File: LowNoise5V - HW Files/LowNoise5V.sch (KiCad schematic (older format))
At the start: 10 parts

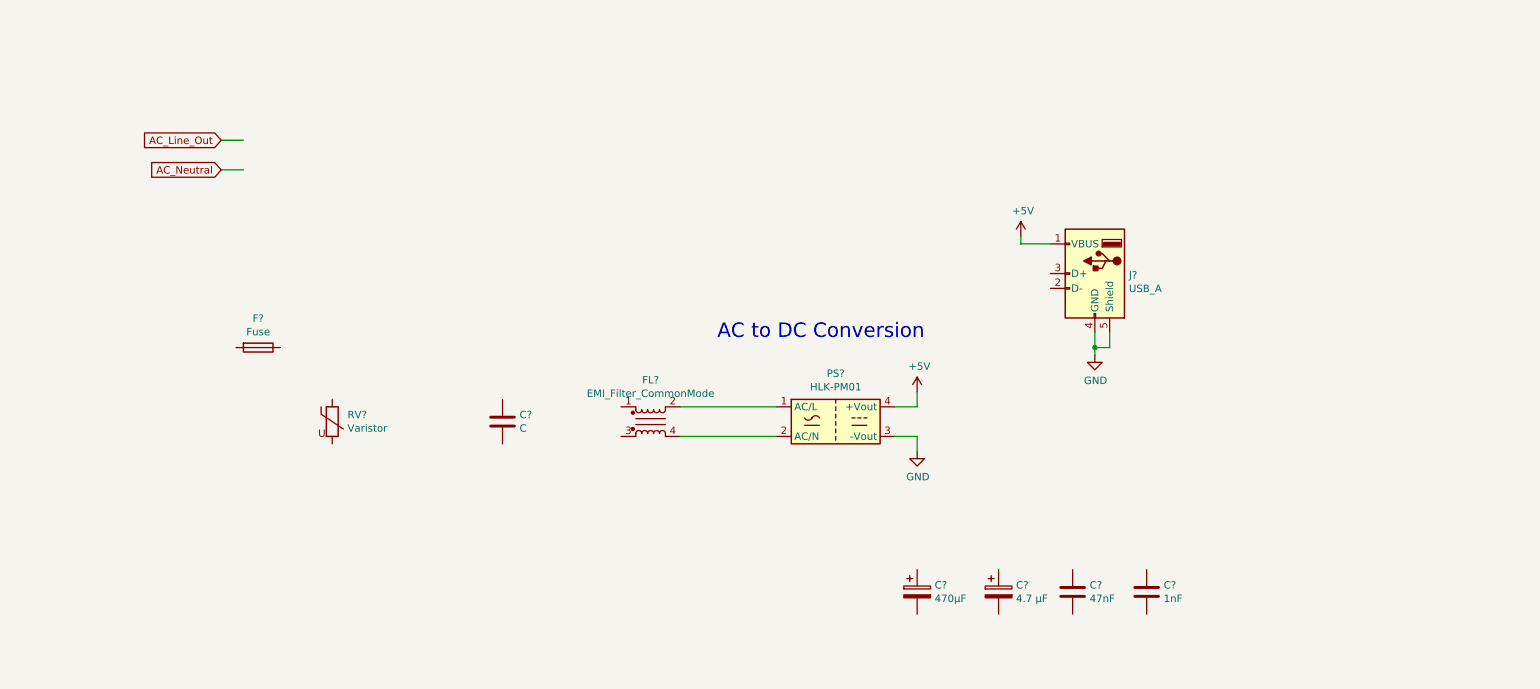
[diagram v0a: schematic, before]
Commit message: Update AC side components with part info
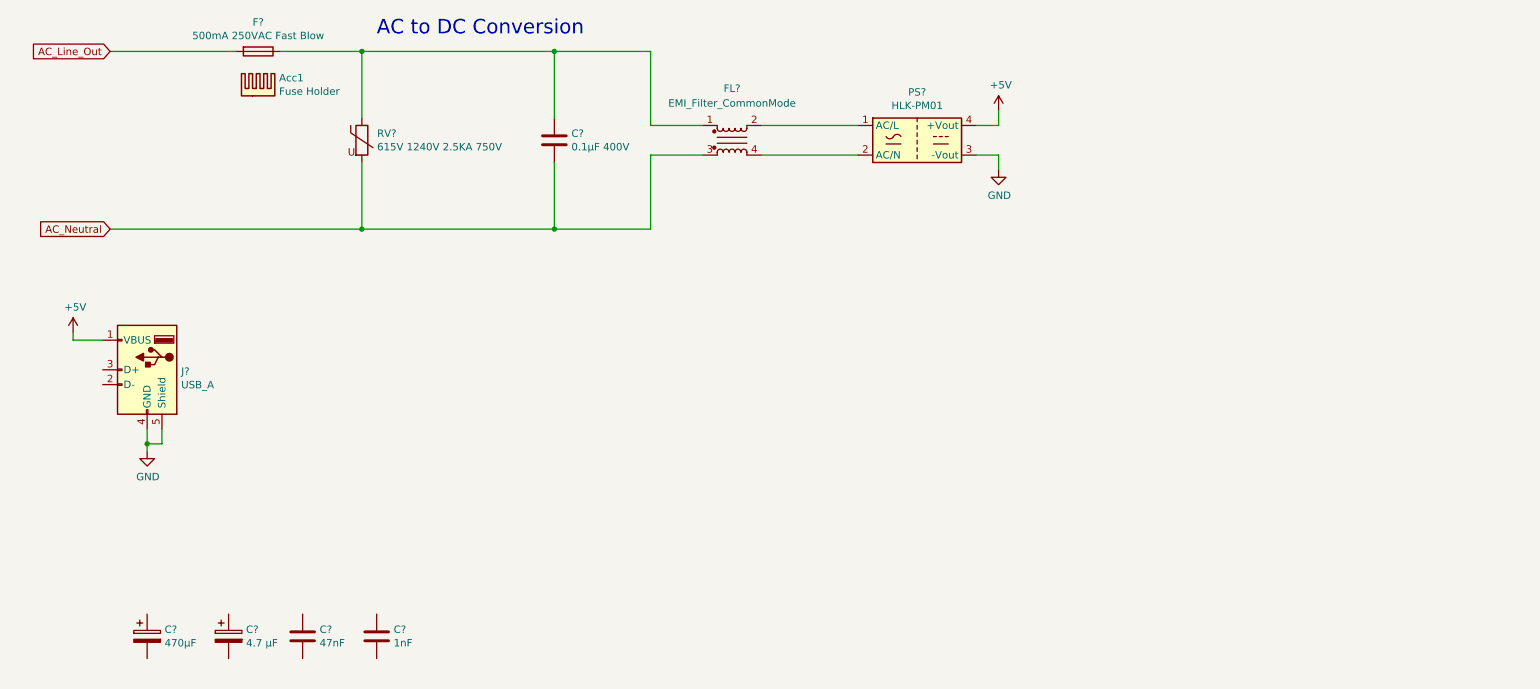
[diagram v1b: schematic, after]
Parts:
- added Acc1: Fuse Holder, symbol Mechanical:Heatsink
- C?: value C -> 0.1µF 400V; Part 1 MF (none) -> Tongfeng; Part 1 MPN (none) -> CL21-0.1uF400V 5%; Part 1 OC (none) -> C281835
- F?: value Fuse -> 500mA 250VAC Fast Blow; Part 1 MF (none) -> Xucheng Elec; Part 1 MPN (none) -> 5F.0500210000R1; Part 1 OC (none) -> C3123
- PS?: MF 1 HI-LINK -> (none); MF 1 MPN HLK-PM01 -> (none); MF 1 Ordering Code C209903 -> (none); Part 1 MF (none) -> HI-LINK; Part 1 MPN (none) -> HLK-PM01; Part 1 OC (none) -> C209903
- RV?: value Varistor -> 615V 1240V 2.5KA 750V; Part 1 MF (none) -> Hongzhi Elec; Part 1 MPN (none) -> 10D751K; Part 1 OC (none) -> C136811
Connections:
- wire segments 14 -> 27
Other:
- moved on the sheet: C?, F?, FL?, J?, PS?, RV?

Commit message: Add DC component part info
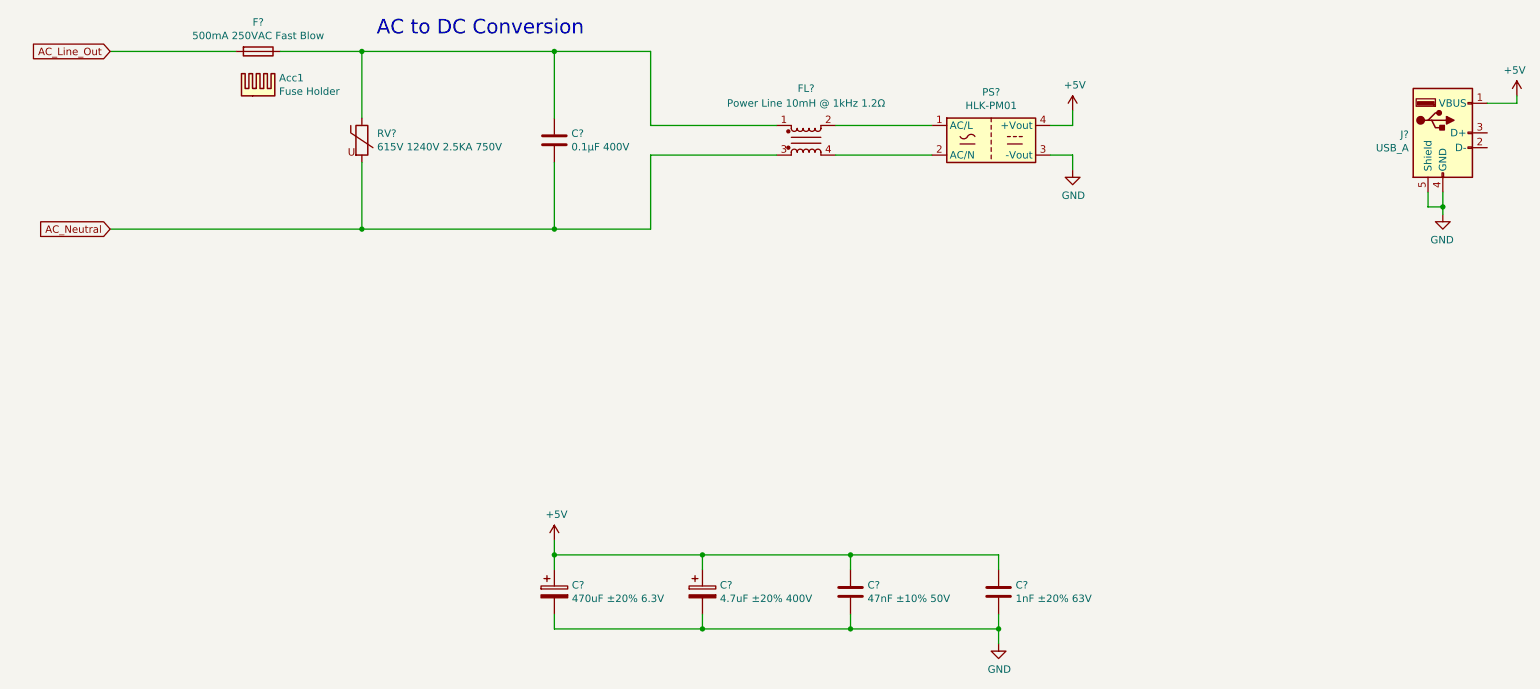
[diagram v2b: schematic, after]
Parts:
- C?: value 470µF -> 470uF ±20% 6.3V; footprint (none) -> Capacitor_THT:CP_Radial_D6.3mm_P2.50mm; Part 1 MF (none) -> Rubycon; Part 1 MPN (none) -> 6.3ZLH470MEFCT16.3X11; Part 1 OC (none) -> C440024
- C?: value 4.7 µF -> 4.7uF ±20% 400V; Part 1 MF (none) -> AISHI(Aihua Group); Part 1 MPN (none) -> EGS2GM4R7E12OT; Part 1 OC (none) -> C106368
- C?: value 47nF -> 47nF ±10% 50V; Part 1 MF (none) -> Dersonic; Part 1 MPN (none) -> CD1H473KC9BER1E000; Part 1 OC (none) -> C263197
- C?: value 1nF -> 1nF ±20% 63V; Part 1 MF (none) -> TORCH; Part 1 MPN (none) -> CT4-0805-2F4-63V-1000pF-M; Part 1 OC (none) -> C123144
- FL?: value EMI_Filter_CommonMode -> Power Line 10mH @ 1kHz 1.2Ω; Part 1 MF (none) -> FH(Guangdong Fenghua Advanced Tech); Part 1 MPN (none) -> UU9.8Y-10mH; Part 1 OC (none) -> C75192
- J?: footprint Connector_USB:USB_A_Molex_67643_Horizontal -> (none); Part 1 OC (none) -> C293351
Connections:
- net +5V: now also C?.1, C?.1, C?.1, C?.1
- net GND: now also C?.2, C?.2, C?.2, C?.2
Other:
- moved on the sheet: C?, FL?, J?, PS?

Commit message: finalize component part selection and populate some footprints
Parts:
- C1: renamed from C?; footprint (none) -> Capacitor_THT:C_Rect_L10.0mm_W4.0mm_P7.50mm_MKS4
- C3: renamed from C?; footprint (none) -> Capacitor_THT:CP_Radial_D6.3mm_P2.50mm
- J1: renamed from J?; footprint (none) -> Connector_USB:USB_A_Molex_67643_Horizontal
- PS1: renamed from PS?; footprint HotPlateController:Converter_ACDC_HiLink_HLK-PMxx -> Converter_ACDC:Converter_ACDC_HiLink_HLK-PMxx
- RV1: renamed from RV?; footprint (none) -> Capacitor_THT:C_Rect_L9.0mm_W9.8mm_P7.50mm_MKT
- gave numbers to parts that had none: 5
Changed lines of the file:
@@
 P 7450 1600
 AR Path="/604F9C77/605057F1" Ref="PS?"  Part="1"
-AR Path="/605057F1" Ref="PS?"  Part="1"
-F 0 "PS?" H 7450 1925 50  0000 C CNN
+AR Path="/605057F1" Ref="PS1"  Part="1"
+F 0 "PS1" H 7450 1925 50  0000 C CNN
 F 1 "HLK-PM01" H 7450 1834 50  0000 C CNN
-F 2 "HotPlateController:Converter_ACDC_HiLink_HLK-PMxx" H 7450 1300 50  0001 C CNN
+F 2 "Converter_ACDC:Converter_ACDC_HiLink_HLK-PMxx" H 7450 1300 50  0001 C CNN
 F 3 "http://www.hlktech.net/product_detail.php?ProId=54" H 7850 1250 50  0001 C CNN
 F 4 "" H 7450 1600 50  0001 C CNN "MF 1"
@@
 P 8000 1800
 AR Path="/604F9C77/605057F7" Ref="#PWR?"  Part="1"
-AR Path="/605057F7" Ref="#PWR?"  Part="1"
-F 0 "#PWR?" H 8000 1550 50  0001 C CNN
+AR Path="/605057F7" Ref="#PWR0101"  Part="1"
+F 0 "#PWR0101" H 8000 1550 50  0001 C CNN
 F 1 "GND" H 8005 1627 50  0000 C CNN
 F 2 "" H 8000 1800 50  0001 C CNN
@@
 P 8000 1400
 AR Path="/604F9C77/605057FD" Ref="#PWR?"  Part="1"
-AR Path="/605057FD" Ref="#PWR?"  Part="1"
-F 0 "#PWR?" H 8000 1250 50  0001 C CNN
+AR Path="/605057FD" Ref="#PWR0102"  Part="1"
+F 0 "#PWR0102" H 8000 1250 50  0001 C CNN
 F 1 "+5V" H 8015 1573 50  0000 C CNN
 F 2 "" H 8000 1400 50  0001 C CNN
@@
 AC to DC Conversion
 $Comp
-L Connector:USB_A J?
+L Connector:USB_A J1
 U 1 1 60505B03
 P 10500 1550
-F 0 "J?" H 10270 1539 50  0000 R CNN
+F 0 "J1" H 10270 1539 50  0000 R CNN
 F 1 "USB_A" H 10270 1448 50  0000 R CNN
-F 2 "" H 10650 1500 50  0001 C CNN
+F 2 "Connector_USB:USB_A_Molex_67643_Horizontal" H 10650 1500 50  0001 C CNN
 F 3 " ~" H 10650 1500 50  0001 C CNN
 F 4 "Molex" H 10500 1550 50  0001 C CNN "Part 1 MF"
@@
 P 11000 1300
 AR Path="/604F9C77/60506A13" Ref="#PWR?"  Part="1"
-AR Path="/60506A13" Ref="#PWR?"  Part="1"
-F 0 "#PWR?" H 11000 1150 50  0001 C CNN
+AR Path="/60506A13" Ref="#PWR0103"  Part="1"
+F 0 "#PWR0103" H 11000 1150 50  0001 C CNN
 F 1 "+5V" H 11015 1473 50  0000 C CNN
 F 2 "" H 11000 1300 50  0001 C CNN
@@
 P 10500 2100
 AR Path="/604F9C77/605077C1" Ref="#PWR?"  Part="1"
-AR Path="/605077C1" Ref="#PWR?"  Part="1"
-F 0 "#PWR?" H 10500 1850 50  0001 C CNN
+AR Path="/605077C1" Ref="#PWR0104"  Part="1"
+F 0 "#PWR0104" H 10500 1850 50  0001 C CNN
 F 1 "GND" H 10505 1927 50  0000 C CNN
 F 2 "" H 10500 2100 50  0001 C CNN
@@
 Connection ~ 10500 2050
 $Comp
-L Device:EMI_Filter_CommonMode FL?
+L Device:EMI_Filter_CommonMode FL1
 U 1 1 605085D5
 P 6200 1600
-F 0 "FL?" H 6200 1950 50  0000 C CNN
+F 0 "FL1" H 6200 1950 50  0000 C CNN
 F 1 "Power Line 10mH @ 1kHz 1.2Ω" H 6200 1850 50  0000 C CNN
 F 2 "" H 6200 1640 50  0001 C CNN
@@
 	7050 1700 6400 1700
 $Comp
-L Device:C C?
+L Device:C C1
 U 1 1 6050D002
 P 4500 1600
-F 0 "C?" H 4615 1646 50  0000 L CNN
+F 0 "C1" H 4615 1646 50  0000 L CNN
 F 1 "0.1µF 400V" H 4615 1555 50  0000 L CNN
-F 2 "" H 4538 1450 50  0001 C CNN
+F 2 "Capacitor_THT:C_Rect_L10.0mm_W4.0mm_P7.50mm_MKS4" H 4538 1450 50  0001 C CNN
 F 3 "~" H 4500 1600 50  0001 C CNN
 F 4 "Tongfeng" H 4500 1600 50  0001 C CNN "Part 1 MF"
@@
 $EndComp
 $Comp
-L Device:Varistor RV?
+L Device:Varistor RV1
 U 1 1 6050DA4F
 P 3200 1600
-F 0 "RV?" H 3303 1646 50  0000 L CNN
+F 0 "RV1" H 3303 1646 50  0000 L CNN
 F 1 "615V 1240V 2.5KA 750V" H 3303 1555 50  0000 L CNN
-F 2 "" V 3130 1600 50  0001 C CNN
+F 2 "Capacitor_THT:C_Rect_L9.0mm_W9.8mm_P7.50mm_MKT" V 3130 1600 50  0001 C CNN
 F 3 "~" H 3200 1600 50  0001 C CNN
 F 4 "Hongzhi Elec" H 3200 1600 50  0001 C CNN "Part 1 MF"
@@
 $EndComp
 $Comp
-L Device:Fuse F?
+L Device:Fuse F1
 U 1 1 6050E1EC
 P 2500 1000
-F 0 "F?" V 2303 1000 50  0000 C CNN
+F 0 "F1" V 2303 1000 50  0000 C CNN
 F 1 "500mA 250VAC Fast Blow" V 2394 1000 50  0000 C CNN
 F 2 "" V 2430 1000 50  0001 C CNN
@@
 $EndComp
 $Comp
-L Device:CP C?
-U 1 1 605107D5
-P 5500 4650
-F 0 "C?" H 5618 4696 50  0000 L CNN
-F 1 "4.7uF ±20% 400V" H 5618 4605 50  0000 L CNN
-F 2 "" H 5538 4500 50  0001 C CNN
-F 3 "~" H 5500 4650 50  0001 C CNN
-F 4 "AISHI(Aihua Group)" H 5500 4650 50  0001 C CNN "Part 1 MF"
-F 5 "EGS2GM4R7E12OT" H 5500 4650 50  0001 C CNN "Part 1 MPN"
-F 6 "C106368" H 5500 4650 50  0001 C CNN "Part 1 OC"
-	1    5500 4650
-	1    0    0    -1
-$EndComp
-$Comp
-L Device:C C?
+L Device:C C4
 U 1 1 605123CB
 P 6500 4650
-F 0 "C?" H 6615 4696 50  0000 L CNN
+F 0 "C4" H 6615 4696 50  0000 L CNN
 F 1 "47nF ±10% 50V" H 6615 4605 50  0000 L CNN
 F 2 "Capacitor_THT:C_Disc_D6.0mm_W2.5mm_P5.00mm" H 6538 4500 50  0001 C CNN
@@
 $EndComp
 $Comp
-L Device:C C?
+L Device:C C5
 U 1 1 60513220
 P 7500 4650
-F 0 "C?" H 7615 4696 50  0000 L CNN
+F 0 "C5" H 7615 4696 50  0000 L CNN
 F 1 "1nF ±20% 63V" H 7615 4605 50  0000 L CNN
 F 2 "Capacitor_THT:C_Disc_D6.0mm_W2.5mm_P5.00mm" H 7538 4500 50  0001 C CNN
@@
 P 4500 4300
 AR Path="/604F9C77/60540DFF" Ref="#PWR?"  Part="1"
-AR Path="/60540DFF" Ref="#PWR?"  Part="1"
-F 0 "#PWR?" H 4500 4150 50  0001 C CNN
+AR Path="/60540DFF" Ref="#PWR0105"  Part="1"
+F 0 "#PWR0105" H 4500 4150 50  0001 C CNN
 F 1 "+5V" H 4515 4473 50  0000 C CNN
 F 2 "" H 4500 4300 50  0001 C CNN
@@
 $EndComp
 $Comp
-L Device:CP C?
+L Device:CP C2
 U 1 1 60510491
 P 4500 4650
-F 0 "C?" H 4618 4696 50  0000 L CNN
+F 0 "C2" H 4618 4696 50  0000 L CNN
 F 1 "470uF ±20% 6.3V" H 4618 4605 50  0000 L CNN
 F 2 "Capacitor_THT:CP_Radial_D6.3mm_P2.50mm" H 4538 4500 50  0001 C CNN
@@
 P 7500 5000
 AR Path="/604F9C77/60563C6A" Ref="#PWR?"  Part="1"
-AR Path="/60563C6A" Ref="#PWR?"  Part="1"
-F 0 "#PWR?" H 7500 4750 50  0001 C CNN
+AR Path="/60563C6A" Ref="#PWR0106"  Part="1"
+F 0 "#PWR0106" H 7500 4750 50  0001 C CNN
 F 1 "GND" H 7505 4827 50  0000 C CNN
 F 2 "" H 7500 5000 50  0001 C CNN
@@
 Wire Wire Line
 	5150 1700 6000 1700
+$Comp
+L Device:CP C3
+U 1 1 605107D5
+P 5500 4650
+F 0 "C3" H 5618 4696 50  0000 L CNN
+F 1 "4.7uF ±20% 400V" H 5618 4605 50  0000 L CNN
+F 2 "Capacitor_THT:CP_Radial_D6.3mm_P2.50mm" H 5538 4500 50  0001 C CNN
+F 3 "~" H 5500 4650 50  0001 C CNN
+F 4 "AISHI(Aihua Group)" H 5500 4650 50  0001 C CNN "Part 1 MF"
+F 5 "EGS2GM4R7E12OT" H 5500 4650 50  0001 C CNN "Part 1 MPN"
+F 6 "C106368" H 5500 4650 50  0001 C CNN "Part 1 OC"
+	1    5500 4650
+	1    0    0    -1
+$EndComp
 $EndSCHEMATC

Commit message: Customize footprints and place more components
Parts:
- added J2: Conn_01x02, TerminalBlock:TerminalBlock_bornier-2_P5.08mm, symbol Connector_Generic:Conn_01x02
- Acc1: footprint (none) -> LowNoise5V:FuseHolder
- FL1: footprint (none) -> LowNoise5V:EMI Choke; symbol Device:EMI_Filter_CommonMode -> LowNoise5V:EMI_Filter_CommonMode
- J1: footprint Connector_USB:USB_A_Molex_67643_Horizontal -> LowNoise5V:USB_A_Molex_67643_Horizontal
- PS1: footprint Converter_ACDC:Converter_ACDC_HiLink_HLK-PMxx -> LowNoise5V:Converter_ACDC_HiLink_HLK-PMxx
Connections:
- net AC_Neutral: now also FL1.4, J2.2 (Pin_2); no longer FL1.3
- net at PS1.2 (AC/N): now also FL1.3; no longer FL1.4
- net AC_Line_Out renamed AC_Line
- net AC_Line: now also J2.1 (Pin_1)
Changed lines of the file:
@@
 F 0 "PS1" H 7450 1925 50  0000 C CNN
 F 1 "HLK-PM01" H 7450 1834 50  0000 C CNN
-F 2 "Converter_ACDC:Converter_ACDC_HiLink_HLK-PMxx" H 7450 1300 50  0001 C CNN
+F 2 "LowNoise5V:Converter_ACDC_HiLink_HLK-PMxx" H 7450 1300 50  0001 C CNN
 F 3 "http://www.hlktech.net/product_detail.php?ProId=54" H 7850 1250 50  0001 C CNN
 F 4 "" H 7450 1600 50  0001 C CNN "MF 1"
@@
 	8000 1700 8000 1800
 Text GLabel 1500 1000 0    50   Input ~ 0
-AC_Line_Out
+AC_Line
 Text GLabel 1500 2200 0    50   Input ~ 0
 AC_Neutral
@@
 F 0 "J1" H 10270 1539 50  0000 R CNN
 F 1 "USB_A" H 10270 1448 50  0000 R CNN
-F 2 "Connector_USB:USB_A_Molex_67643_Horizontal" H 10650 1500 50  0001 C CNN
+F 2 "LowNoise5V:USB_A_Molex_67643_Horizontal" H 10650 1500 50  0001 C CNN
 F 3 " ~" H 10650 1500 50  0001 C CNN
 F 4 "Molex" H 10500 1550 50  0001 C CNN "Part 1 MF"
@@
 Connection ~ 10500 2050
 $Comp
-L Device:EMI_Filter_CommonMode FL1
+L LowNoise5V:EMI_Filter_CommonMode FL1
 U 1 1 605085D5
 P 6200 1600
 F 0 "FL1" H 6200 1950 50  0000 C CNN
 F 1 "Power Line 10mH @ 1kHz 1.2Ω" H 6200 1850 50  0000 C CNN
-F 2 "" H 6200 1640 50  0001 C CNN
+F 2 "LowNoise5V:EMI Choke" H 6200 1640 50  0001 C CNN
 F 3 "~" H 6200 1640 50  0001 C CNN
 F 4 "FH(Guangdong Fenghua Advanced Tech)" H 6200 1600 50  0001 C CNN "Part 1 MF"
@@
 Connection ~ 4500 2200
 Wire Wire Line
-	2350 1000 1500 1000
+	2350 1000 1850 1000
 Wire Wire Line
 	2650 1000 3200 1000
 Wire Wire Line
-	1500 2200 3200 2200
+	1500 2200 1850 2200
 Wire Wire Line
 	3200 1450 3200 1000
@@
 F 0 "Acc1" H 2641 1421 50  0000 L CNN
 F 1 "Fuse Holder" H 2641 1330 50  0000 L CNN
-F 2 "" H 2512 1300 50  0001 C CNN
+F 2 "LowNoise5V:FuseHolder" H 2512 1300 50  0001 C CNN
 F 3 "~" H 2512 1300 50  0001 C CNN
 F 4 "HONGJU" H 2500 1300 50  0001 C CNN "Part 1 MF"
@@
 	1    0    0    -1
 $EndComp
+$Comp
+L Connector_Generic:Conn_01x02 J2
+U 1 1 6058E947
+P 1300 1550
+F 0 "J2" H 1218 1767 50  0000 C CNN
+F 1 "Conn_01x02" H 1218 1676 50  0000 C CNN
+F 2 "TerminalBlock:TerminalBlock_bornier-2_P5.08mm" H 1300 1550 50  0001 C CNN
+F 3 "~" H 1300 1550 50  0001 C CNN
+	1    1300 1550
+	-1   0    0    -1
+$EndComp
+Wire Wire Line
+	1500 1550 1850 1550
+Wire Wire Line
+	1850 1550 1850 1000
+Connection ~ 1850 1000
+Wire Wire Line
+	1850 1000 1500 1000
+Wire Wire Line
+	1500 1650 1850 1650
+Wire Wire Line
+	1850 1650 1850 2200
+Connection ~ 1850 2200
+Wire Wire Line
+	1850 2200 3200 2200
 $EndSCHEMATC
